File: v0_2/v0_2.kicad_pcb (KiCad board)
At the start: 2 copper layers, 169.4 x 91.6 mm, 49 parts, among them IC1 RASPBERRY_PI_PICO_W, IC2 BH1750FVI-TR, IC3 AP2138N-3.3TRG1, J1 S2B-PH-SM4-TB_LF__SN_, J2 HYCW110-TF10-180B, J3 Conn_01x09_Pin, J4 SM04B-SRSS-TB, Q1 DMG2301L-7, Q2 DMG2301L-7, Q3 DMG2301L-7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

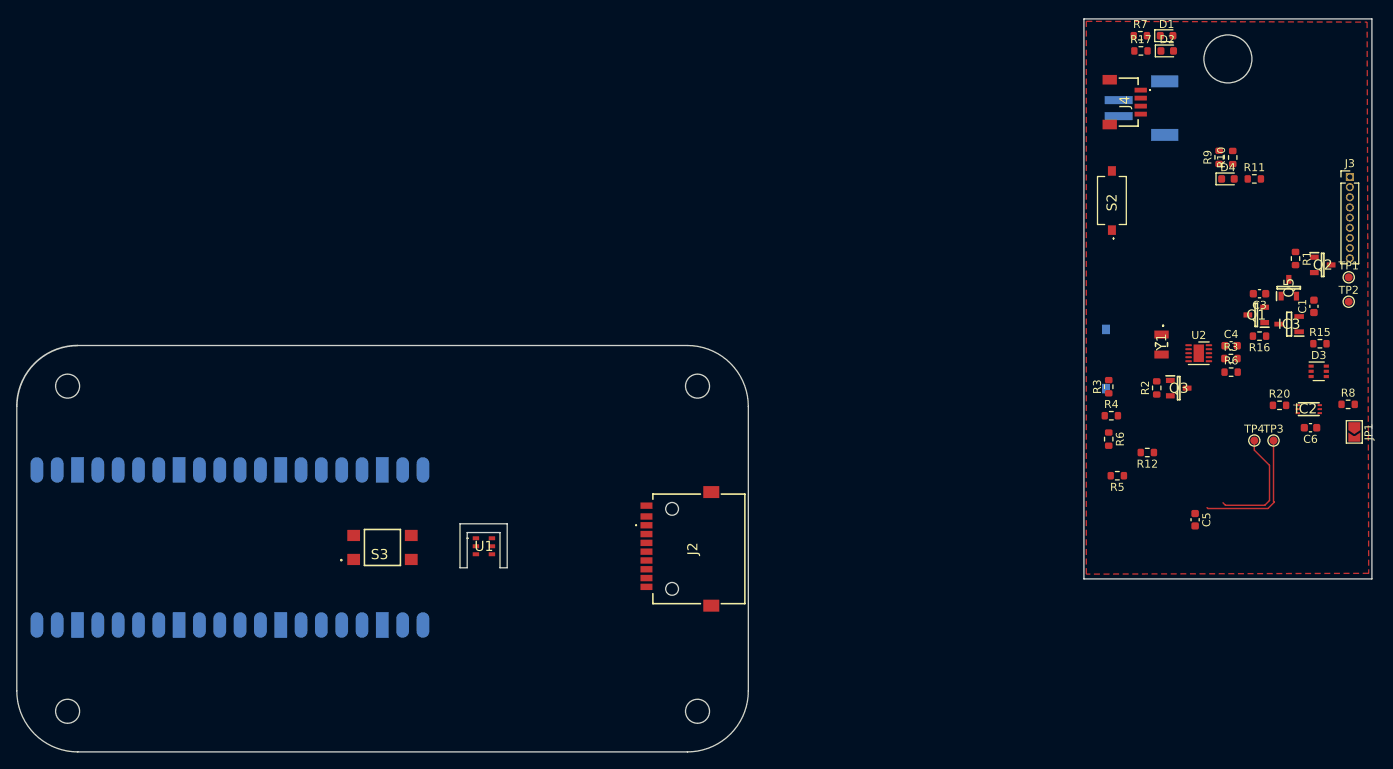
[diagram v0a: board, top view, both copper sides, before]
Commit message: add name and button part
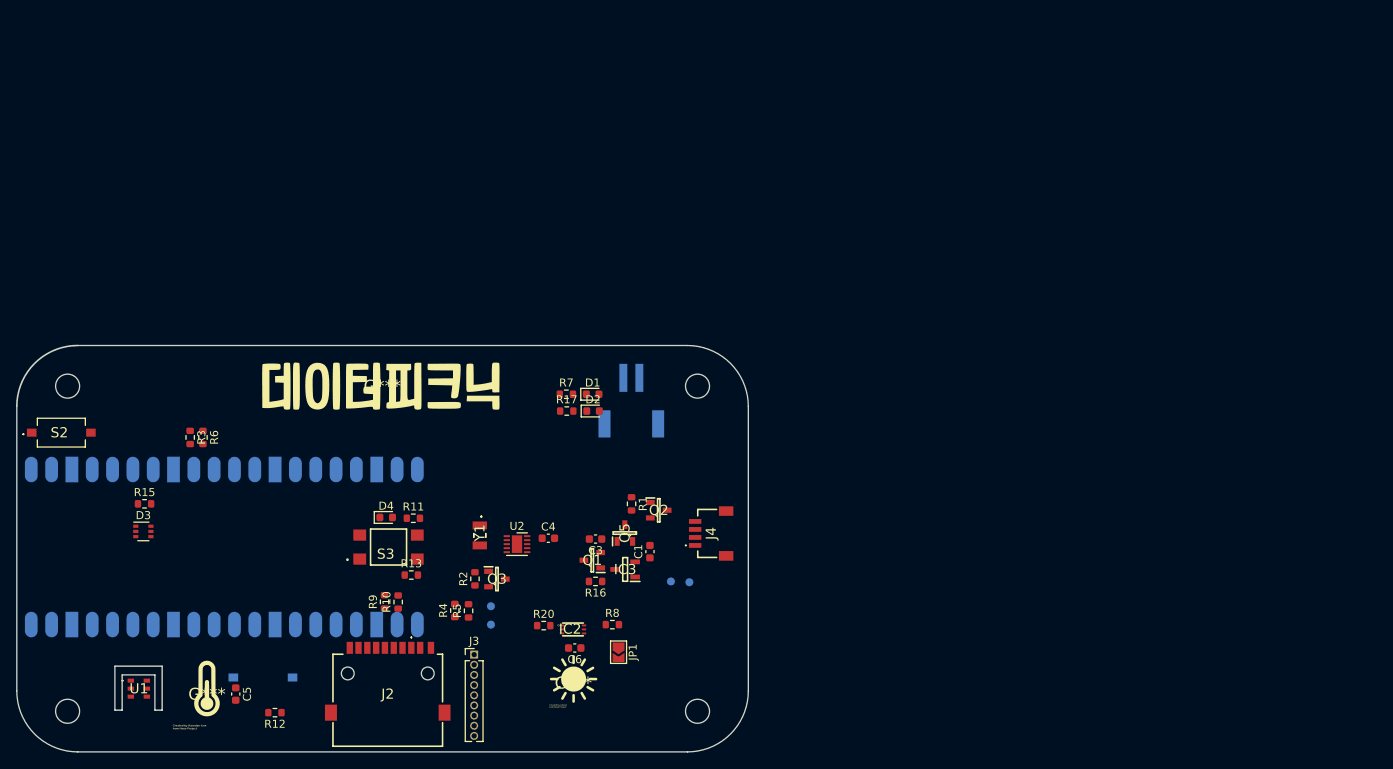
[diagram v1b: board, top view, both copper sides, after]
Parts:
- removed the R3 at (250.9, 65.4)
- removed the R6 at (250.9, 67.1)
- added G***: LOGO, Graphics:temperature_logo_v2, F.Cu at (122.9, 107.4)
- added G***: LOGO, Graphics:light_logo_v3, F.Cu at (168.7, 106.0)
- added G***: LOGO, Graphics:Datapicnic_v2, F.Cu at (144.8, 68.9)
- added R13: 10K, Resistor_SMD:R_0603_1608Metric, F.Cu at (148.4, 92.5)
- TP1, TP2, TP3, TP4: moved to B.Cu
- moved R15 148.3 mm to (115.1, 83.6)
- moved D3 148.3 mm to (114.9, 87.0)
- moved S2 134.5 mm to (104.7, 74.7), turned to 0 degrees
- moved J3 124.7 mm to (156.3, 102.5)
- moved C5 121.9 mm to (126.5, 107.4)
- moved R10 118.2 mm to (146.8, 95.9)
- moved R9 118.2 mm to (145.1, 95.8)
- moved R3 115.0 mm to (120.8, 75.3), turned to -90 degrees
- moved TP1 114.8 mm to (158.4, 96.4), turned to 180 degrees
- moved TP2 114.6 mm to (158.4, 98.7), turned to 180 degrees
- moved R12 113.8 mm to (131.4, 109.7)
- moved D4 113.4 mm to (145.3, 85.3)
- moved R11 113.4 mm to (148.7, 85.4)
- moved R6 113.2 mm to (122.4, 75.3)
- moved S1 112.6 mm to (129.9, 105.3), turned to 180 degrees
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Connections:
- S3 pad 1: unconnected-(S3-Pad1) -> /Button
- S3 pad 2: GND -> Net-(R13-Pad2)
- S3 pad 3: /Button -> unconnected-(S3-Pad3)
- S3 pad 4: unconnected-(S3-Pad4) -> +3.3V
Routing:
- net /I2C1_SCL: track 16.5 -> 0.00 mm
- net /I2C1_SDA: track 14.5 -> 0.00 mm
- removed copper zone on F.Cu, net GND
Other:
- board size 169.4 x 91.6 mm -> 91.4 x 50.8 mm
- board text added: "RESET"

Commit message: power line
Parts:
- removed G***: LOGO, Graphics:temperature_logo_v2
- removed G***: LOGO, Graphics:light_logo_v3
- removed G***: LOGO, Graphics:Datapicnic_v2
- removed J3: Conn_01x09_Pin, Connector_PinHeader_1.27mm:PinHeader_1x09_P1.27mm_Vertical
- added J5: Screw_Terminal_01x03, TerminalBlock:TerminalBlock_Altech_AK300-3_P5.00mm, F.Cu at (140.3, 70.5)
- added J6: Conn_01x02_Pin, Connector_PinHeader_1.27mm:PinHeader_1x02_P1.27mm_Vertical, F.Cu at (167.8, 66.5)
- added R14: 4K7, Resistor_SMD:R_0603_1608Metric, F.Cu at (134.5, 75.3)
- added TP10: TestPoint, TestPoint:TestPoint_Pad_D1.0mm, F.Cu at (104.6, 104.0)
- added TP11: TestPoint, TestPoint:TestPoint_Pad_D1.0mm, F.Cu at (178.2, 95.6)
- added TP12: TestPoint, TestPoint:TestPoint_Pad_D1.0mm, F.Cu at (157.4, 75.6)
- added TP5: TestPoint, TestPoint:TestPoint_Pad_D1.0mm, F.Cu at (158.5, 102.8)
- added TP6: TestPoint, TestPoint:TestPoint_Pad_D1.0mm, F.Cu at (158.5, 105.8)
- added TP7: TestPoint, TestPoint:TestPoint_Pad_D1.0mm, F.Cu at (158.5, 108.8)
- added TP8: TestPoint, TestPoint:TestPoint_Pad_D1.0mm, F.Cu at (158.5, 111.9)
- added TP9: TestPoint, TestPoint:TestPoint_Pad_D1.0mm, F.Cu at (107.7, 104.0)
- added U3: DS18B20, Package_TO_SOT_THT:TO-92_Inline, F.Cu at (131.5, 71.2)
- TP1, TP2, TP3, TP4: moved to F.Cu
- moved D3 57.1 mm to (171.8, 82.3)
- moved R15 57.1 mm to (172.0, 78.9)
- moved R12 22.1 mm to (109.3, 108.7)
- moved TP4 6.29 mm to (187.1, 93.8), turned to 0 degrees
- moved R1 5.19 mm to (171.5, 86.3), turned to 0 degrees
- moved TP1 4.30 mm to (158.3, 100.7), turned to 0 degrees
- moved R10 1.94 mm to (144.8, 95.8), turned to -90 degrees
- moved R9 1.46 mm to (146.5, 95.8), turned to -90 degrees
- moved TP3 1.30 mm to (184.4, 93.7), turned to 0 degrees
- moved Q5 0.60 mm to (175.1, 86.7), turned to -90 degrees
- turned TP2 to 0 degrees
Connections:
- IC1 pad 33: unconnected-(IC1-GND/AGND-Pad33) -> GND
- IC1 pad 34: unconnected-(IC1-GP28/ADC2-Pad34) -> /DQ
- Q5 pad 1: /LDO/VSYS_EN -> /VSYS_EN
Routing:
- net +3.3V: track 0.00 -> 152.6 mm
- net +BATT: track 0.00 -> 66.3 mm
- net V+_A0: track 0.00 -> 42.3 mm
- net /LDO/VIN: track 0.00 -> 5.45 mm
